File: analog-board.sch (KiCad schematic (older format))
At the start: 496 parts, among them J1 AC IN, J2 OUT, J3 CONN_20X2, P2 CONN_01X02, Q1 2N3906, Q10 2N3906, Q11 2N3906, Q12 2N3906, Q13 2N3906, Q14 2N3906, Q15 2N3906, Q16 2N3906, Q17 NPN, Q18 NPN, Q19 J111, Q2 2N3906, Q20 2N3906, Q3 2N3906, Q4 2N3906, Q5 2N3906, Q6 BCM857BS, Q7 2N3906, Q8 2N3906, Q9 2N3906, U1 LM13700, U10 ADR01, U11 DG212B, U12 DG212B, U13 DG408, U14 DG408, U15 TL072-, U16 DG408, U17 DG408, U18 LM13700, U19 LM13700, U2 LM13700, U20 74HC75, U21 TL072-, U22 TL074-, U23 TL074-, U24 TL074-, U25 TL074-, U26 TL072-, U27 TL074-, U28 TL074-, U29 LM13700, U3 LM13700, U30 LM13700, U31 TL074-, U32 LM13700, U33 TL074-, U34 TL074-, U35 TL074-, U36 74LV573, U38 0 - 10V, U39 TL074-, U4 DG212B, U40 DG419, U41 0 - 10V, U42 10 - 0V, U43 LM7812, U44 LM7912, U45 DG408, U46 7805, U5 TL074-, U6 AD5556, U7 TL072-, U8 TL074-, U9 AD8672

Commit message: LFO TUNE now connected to S&H clock through R215
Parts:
- added R215: 10K, symbol R_US
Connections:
- net LFO TUNE: now also R215.1; no longer C102.1, LFO1.9, R210.2
- net at D4.2 (K), TP25.1, U39.8: now also R215.2
- new net: C102.1, LFO1.9, R210.2
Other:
- note added: "*NOTE: C47 and C48 values: need\nto experiment more with C47 and \nC48 values. Changee to dual\nfootprint 0805 and TH."
- note added: "Can probably\nget rid of mixer\nVCA trimmers"
- note added: "Can probably\nget rid of volume\nVCA trimmer"
- note added: "Move C100 to after\nvolume VCA?"
- note added: "NP0 or FILM\n"
- note added: "S&H CLOCK"
- note removed: "*NOTE: C47 and C48 values: need\nto experiment more with C47 and \nC48 values. Change to dual\nfootprint 0805 and TH."
- note removed: "NP0 or FILM\nNeed to change to larger footprint here!"
- note removed: "Need to change to\nlarger footprint here!"
- moved on the sheet: TP25
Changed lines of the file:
@@
 $EndComp
 Text Notes 39000 7350 0    60   ~ 0
-NP0 or FILM\nNeed to change to larger footprint here!
+NP0 or FILM\n
 $Comp
 L GND #PWR0114
@@
 L CONN_1 TP25
 U 1 1 5453F2E4
-P 38450 8050
-F 0 "TP25" H 38530 8050 40  0000 L CNN
-F 1 "CONN_1" H 38450 8150 30  0001 C CNN
-F 2 "~" H 38450 8050 60  0000 C CNN
-F 3 "~" H 38450 8050 60  0000 C CNN
-	1    38450 8050
-	1    0    0    -1
+P 38650 7700
+F 0 "TP25" H 38730 7700 40  0000 L CNN
+F 1 "CONN_1" H 38650 7800 30  0001 C CNN
+F 2 "~" H 38650 7700 60  0000 C CNN
+F 3 "~" H 38650 7700 60  0000 C CNN
+	1    38650 7700
+	0    -1   -1   0
 $EndComp
-Text GLabel 36400 4700 2    60   Output ~ 0
-LFO TUNE
 Text Notes 40500 3900 0    60   ~ 0
 S&H
@@
 Text Notes 42450 7050 1    60   ~ 0
 Note: for ease of PCB layout order\nof mux addressing is not sequential
-Text Notes 18400 9150 0    60   ~ 0
-Need to change to\nlarger footprint here!
-Text Notes 18300 11000 0    60   ~ 0
-Need to change to\nlarger footprint here!
 Text Notes 14600 13800 0    60   ~ 0
 Changed to 47K to\nprevent clipping
@@
 *NOTE: jumper 1K output resistor\non EG2 module; it forms a divider \nwith input resistors to EG2 \nmodulation depth VCAs
 Text Notes 16450 11100 0    60   ~ 0
-*NOTE: C47 and C48 values: need\nto experiment more with C47 and \nC48 values. Change to dual\nfootprint 0805 and TH.
+*NOTE: C47 and C48 values: need\nto experiment more with C47 and \nC48 values. Changee to dual\nfootprint 0805 and TH.
 Text Notes 31500 31750 0    60   ~ 0
 External gate input doesn't work here.\nProbably because OR gate on digital board\ncan sink and source current, so holds output \nlow when external gate is applied?
@@
 Connection ~ 37000 8150
 Wire Wire Line
-	31650 4700 36400 4700
-Wire Wire Line
 	31650 4700 31650 8150
 Wire Wire Line
 	31650 8150 35900 8150
 Connection ~ 40250 5950
-Connection ~ 36150 4700
 Wire Wire Line
 	42200 4600 42200 5200
@@
 Text Notes 12300 20800 0    60   ~ 0
 PULSE output\ndivider network\nto get 10 Vpp
+$Comp
+L R_US R215
+U 1 1 559CB5A4
+P 39000 8050
+F 0 "R215" V 39080 8050 50  0000 C CNN
+F 1 "10K" V 38920 8050 50  0000 C CNN
+F 2 "" H 39000 8050 60  0000 C CNN
+F 3 "" H 39000 8050 60  0000 C CNN
+	1    39000 8050
+	0    1    1    0
+$EndComp
+Text GLabel 39300 8050 2    60   Output ~ 0
+LFO TUNE
+Wire Wire Line
+	38300 8050 38800 8050
+Wire Wire Line
+	38650 7850 38650 8050
+Connection ~ 38650 8050
+Text Notes 38750 7750 0    60   ~ 0
+S&H CLOCK
+Wire Wire Line
+	39200 8050 39300 8050
+Wire Wire Line
+	36150 4700 31650 4700
+Text Notes 17650 15850 0    60   ~ 0
+Can probably\nget rid of mixer\nVCA trimmers
+Text Notes 19500 18150 0    60   ~ 0
+Can probably\nget rid of mixer\nVCA trimmers
+Text Notes 17600 20750 0    60   ~ 0
+Can probably\nget rid of mixer\nVCA trimmers
+Text Notes 37650 17800 0    60   ~ 0
+Can probably\nget rid of volume\nVCA trimmer
+Text Notes 38650 16500 0    60   ~ 0
+Can probably\nget rid of volume\nVCA trimmer
+Text Notes 35450 16200 0    60   ~ 0
+Move C100 to after\nvolume VCA?
 $EndSCHEMATC

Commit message: moved final DC blocking cap to output of volume VCA, deleted ring output resistor to J2
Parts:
- removed R205: 1K, symbol R_US
- added C134: 22µ, ~, symbol CP_US
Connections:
- net at C111.1, R202.2, R204.1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: no longer TP26.1
- net at R200.2, U32.5: now also C134.1 (+); no longer R202.1
- new net: C134.2 (-), R202.1, TP26.1
- no-connect marks 17 -> 18
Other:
- note added: "Jumper C100 and try\nC134 as DC blocker"
- note added: "Plugging TS jack in shorts ring to GND\nSo dual output to ring has been removed"
- note added: "Where did the idea for \nthis final buffer come \nfrom? P5 uses non-\ninverting buffer. This\nlooks more like JP8\noutput amplifier."
- note removed: "J2 pins mixed up, results in \noutput being shorted to ground!"
- note removed: "Move C100 to after\nvolume VCA?"
- moved on the sheet: C111, J2, R202, R204, R39, TP26, U35D
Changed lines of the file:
@@
 L R_US R39
 U 1 1 5453E97B
-P 40700 16750
-F 0 "R39" V 40900 16750 50  0000 C CNN
-F 1 "1K" V 40800 16750 50  0000 C CNN
-F 2 "" H 40700 16750 60  0000 C CNN
-F 3 "" H 40700 16750 60  0000 C CNN
-	1    40700 16750
+P 41150 16750
+F 0 "R39" V 41350 16750 50  0000 C CNN
+F 1 "1K" V 41250 16750 50  0000 C CNN
+F 2 "" H 41150 16750 60  0000 C CNN
+F 3 "" H 41150 16750 60  0000 C CNN
+	1    41150 16750
 	0    -1   -1   0
 $EndComp
@@
 L GND #PWR073
 U 1 1 5453EA14
-P 39250 17050
-F 0 "#PWR073" H 39250 17050 30  0001 C CNN
-F 1 "GND" H 39250 16980 30  0001 C CNN
-F 2 "~" H 39250 17050 60  0000 C CNN
-F 3 "~" H 39250 17050 60  0000 C CNN
-	1    39250 17050
+P 39700 17050
+F 0 "#PWR073" H 39700 17050 30  0001 C CNN
+F 1 "GND" H 39700 16980 30  0001 C CNN
+F 2 "~" H 39700 17050 60  0000 C CNN
+F 3 "~" H 39700 17050 60  0000 C CNN
+	1    39700 17050
 	1    0    0    -1
 $EndComp
@@
 L R_US R204
 U 1 1 5453EA1A
-P 39900 15800
-F 0 "R204" V 39980 15800 50  0000 C CNN
-F 1 "100K" V 39820 15800 50  0000 C CNN
-F 2 "" H 39900 15800 60  0000 C CNN
-F 3 "" H 39900 15800 60  0000 C CNN
-	1    39900 15800
+P 40350 15750
+F 0 "R204" V 40430 15750 50  0000 C CNN
+F 1 "100K" V 40270 15750 50  0000 C CNN
+F 2 "" H 40350 15750 60  0000 C CNN
+F 3 "" H 40350 15750 60  0000 C CNN
+	1    40350 15750
 	0    -1   -1   0
 $EndComp
@@
 L C_US C111
 U 1 1 5453EA20
-P 39900 15450
-F 0 "C111" H 39950 15550 50  0000 L CNN
-F 1 "100pF" H 39950 15350 50  0000 L CNN
-F 2 "~" H 39900 15450 60  0000 C CNN
-F 3 "~" H 39900 15450 60  0000 C CNN
-	1    39900 15450
+P 40350 15450
+F 0 "C111" H 40400 15550 50  0000 L CNN
+F 1 "100pF" H 40400 15350 50  0000 L CNN
+F 2 "~" H 40350 15450 60  0000 C CNN
+F 3 "~" H 40350 15450 60  0000 C CNN
+	1    40350 15450
 	0    -1   -1   0
 $EndComp
@@
 L JACK_MONO_SW J2
 U 1 1 5453EA99
-P 41250 16900
-F 0 "J2" H 40700 16800 60  0000 C CNN
-F 1 "OUT" H 41000 17100 60  0000 C CNN
-F 2 "~" H 41150 16900 60  0000 C CNN
-F 3 "~" H 41150 16900 60  0000 C CNN
-	1    41250 16900
+P 41700 16900
+F 0 "J2" H 41150 16800 60  0000 C CNN
+F 1 "OUT" H 41450 17100 60  0000 C CNN
+F 2 "~" H 41600 16900 60  0000 C CNN
+F 3 "~" H 41600 16900 60  0000 C CNN
+	1    41700 16900
 	-1   0    0    1
 $EndComp
@@
 L GND #PWR082
 U 1 1 5453EAA0
-P 40900 17250
-F 0 "#PWR082" H 40900 17250 30  0001 C CNN
-F 1 "GND" H 40900 17180 30  0001 C CNN
-F 2 "~" H 40900 17250 60  0000 C CNN
-F 3 "~" H 40900 17250 60  0000 C CNN
-	1    40900 17250
+P 41350 17250
+F 0 "#PWR082" H 41350 17250 30  0001 C CNN
+F 1 "GND" H 41350 17180 30  0001 C CNN
+F 2 "~" H 41350 17250 60  0000 C CNN
+F 3 "~" H 41350 17250 60  0000 C CNN
+	1    41350 17250
 	1    0    0    -1
 $EndComp
@@
 L R_US R202
 U 1 1 546C49C0
-P 38900 16650
-F 0 "R202" V 38980 16650 50  0000 C CNN
-F 1 "100K" V 38820 16650 50  0000 C CNN
-F 2 "" H 38900 16650 60  0000 C CNN
-F 3 "" H 38900 16650 60  0000 C CNN
-	1    38900 16650
+P 39350 16650
+F 0 "R202" V 39430 16650 50  0000 C CNN
+F 1 "100K" V 39270 16650 50  0000 C CNN
+F 2 "" H 39350 16650 60  0000 C CNN
+F 3 "" H 39350 16650 60  0000 C CNN
+	1    39350 16650
 	0    -1   -1   0
 $EndComp
@@
 L CONN_1 TP26
 U 1 1 546C5BBD
-P 39250 15300
-F 0 "TP26" H 39330 15300 40  0000 L CNN
-F 1 "CONN_1" H 39250 15400 30  0001 C CNN
-F 2 "~" H 39250 15300 60  0000 C CNN
-F 3 "~" H 39250 15300 60  0000 C CNN
-	1    39250 15300
+P 39100 15350
+F 0 "TP26" H 39180 15350 40  0000 L CNN
+F 1 "CONN_1" H 39100 15450 30  0001 C CNN
+F 2 "~" H 39100 15350 60  0000 C CNN
+F 3 "~" H 39100 15350 60  0000 C CNN
+	1    39100 15350
 	0    -1   -1   0
 $EndComp
@@
 L TL074- U35
 U 4 1 548B1C06
-P 39850 16750
-F 0 "U35" H 39900 16950 60  0000 C CNN
-F 1 "TL074-" H 40000 16550 50  0000 C CNN
-F 2 "~" H 39850 16750 60  0000 C CNN
-F 3 "~" H 39850 16750 60  0000 C CNN
-	4    39850 16750
+P 40300 16750
+F 0 "U35" H 40350 16950 60  0000 C CNN
+F 1 "TL074-" H 40450 16550 50  0000 C CNN
+F 2 "~" H 40300 16750 60  0000 C CNN
+F 3 "~" H 40300 16750 60  0000 C CNN
+	4    40300 16750
 	1    0    0    -1
 $EndComp
@@
 NoConn ~ 37150 24250
 $Comp
-L R_US R205
-U 1 1 549A3192
-P 40700 16900
-F 0 "R205" V 40550 16900 50  0000 C CNN
-F 1 "1K" V 40620 16900 50  0000 C CNN
-F 2 "" H 40700 16900 60  0000 C CNN
-F 3 "" H 40700 16900 60  0000 C CNN
-	1    40700 16900
-	0    -1   -1   0
-$EndComp
-$Comp
 L CONN_01X02 P2
 U 1 1 54961D96
@@
 Text Notes 6000 24250 0    60   ~ 0
 bias PWM MOD \nCVs down -5V
-Text Notes 40700 16450 0    60   ~ 0
-J2 pins mixed up, results in \noutput being shorted to ground!
+Text Notes 41150 16450 0    60   ~ 0
+Plugging TS jack in shorts ring to GND\nSo dual output to ring has been removed
 Text Notes 35600 30650 0    60   ~ 0
 *NOTE: jumper 1K output resistor\non EG2 module; it forms a divider \nwith input resistors to EG2 \nmodulation depth VCAs
@@
 	35200 16500 35450 16500
 Wire Wire Line
-	39100 16650 39350 16650
+	39550 16650 39800 16650
 Wire Wire Line
-	39350 16850 39250 16850
+	39800 16850 39700 16850
 Wire Wire Line
-	39250 16850 39250 17050
+	39700 16850 39700 17050
 Wire Wire Line
-	39700 15800 39250 15800
+	40150 15750 39700 15750
 Wire Wire Line
-	39250 15450 39250 16650
-Connection ~ 39250 16650
+	39700 15450 39700 16650
+Connection ~ 39700 16650
 Wire Wire Line
-	40100 15800 40500 15800
+	40550 15750 40950 15750
 Wire Wire Line
-	40500 15450 40500 16900
+	40150 15450 39700 15450
+Connection ~ 39700 15750
 Wire Wire Line
-	39700 15450 39250 15450
-Connection ~ 39250 15800
-Wire Wire Line
-	40100 15450 40500 15450
-Connection ~ 40500 15800
+	40550 15450 40950 15450
+Connection ~ 40950 15750
 Wire Wire Line
 	35850 16500 35950 16500
@@
 	35000 3900 35000 4050
 Wire Wire Line
-	41000 17050 40900 17050
+	41450 17050 41350 17050
 Wire Wire Line
-	40900 17050 40900 17250
+	41350 17050 41350 17250
 Wire Wire Line
 	12150 19900 12150 20650
@@
 	33750 21350 33750 18850
 Wire Wire Line
-	40500 16750 40350 16750
-Connection ~ 40500 16750
+	40950 16750 40800 16750
+Connection ~ 40950 16750
 Wire Notes Line
 	29900 27600 37400 27600
@@
 	38200 15500 38200 15800
 Wire Wire Line
-	38350 16650 38700 16650
+	38350 16650 38650 16650
 Wire Wire Line
 	38500 16650 38500 16850
@@
 	37150 17700 37250 17700
 Wire Wire Line
-	41000 16750 40900 16750
+	41450 16750 41350 16750
 Wire Wire Line
 	27200 28600 27000 28600
@@
 	5250 23600 5250 23550
 Wire Wire Line
-	41000 16900 40900 16900
+	41450 16900 41350 16900
 Wire Wire Line
 	37550 23400 39250 23400
@@
 Text Notes 37650 17800 0    60   ~ 0
 Can probably\nget rid of volume\nVCA trimmer
-Text Notes 38650 16500 0    60   ~ 0
-Can probably\nget rid of volume\nVCA trimmer
 Text Notes 35450 16200 0    60   ~ 0
-Move C100 to after\nvolume VCA?
+Jumper C100 and try\nC134 as DC blocker
+$Comp
+L CP_US C134
+U 1 1 55A0FDA4
+P 38850 16650
+F 0 "C134" H 38900 16750 50  0000 L CNN
+F 1 "22µ" H 38900 16550 50  0000 L CNN
+F 2 "~" H 38850 16650 60  0000 C CNN
+F 3 "~" H 38850 16650 60  0000 C CNN
+	1    38850 16650
+	0    -1   -1   0
+$EndComp
+Wire Wire Line
+	40950 15450 40950 16750
+NoConn ~ 41350 16900
+Text Notes 39800 16450 0    60   ~ 0
+Where did the idea for \nthis final buffer come \nfrom? P5 uses non-\ninverting buffer. This\nlooks more like JP8\noutput amplifier.
+Wire Wire Line
+	39050 16650 39150 16650
+Wire Wire Line
+	39100 15500 39100 16650
+Connection ~ 39100 16650
 $EndSCHEMATC

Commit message: added note about changing R11 and R117 to 470K for VCO1 and FIL cutoff modulation by EG2
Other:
- note added: "Changed to 470K\nto minimize offset"
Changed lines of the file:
@@
 LIBS:MySynthParts
 LIBS:analog-board-cache
-EELAYER 25 0
+EELAYER 24 0
 EELAYER END
 $Descr E 44000 34000
@@
 	39100 15500 39100 16650
 Connection ~ 39100 16650
+Text Notes 2500 7650 0    60   ~ 0
+Changed to 470K\nto minimize offset
+Text Notes 24600 8700 0    60   ~ 0
+Changed to 470K\nto minimize offset
 $EndSCHEMATC

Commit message: added TUNE COMPARATOR in schematic, need to route in PCB
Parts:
- added C?: 10p, ~, symbol C_US
- added D?: 1N4148, ~, symbol DIODE
- added R?: 270K, ~, symbol R_US
- added R?: 22K, ~, symbol R_US
- added R?: 10K, ~, symbol R_US
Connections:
- net +12V: now also R?.2
- net GND: now also R?.1, R?.2; no longer U26.5 (+)
- net TUNE: now also D?.2 (K), R?.2; no longer C100.1 (+), TP24.1, VCFA1.10 (OUT)
- net at U26.6 (-): now also R?.1, R?.1; no longer U26.7
- new net: C100.1 (+), C?.1, TP24.1, U26.5 (+), VCFA1.10 (OUT)
- new net: C?.2, D?.1 (A), U26.7
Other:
- note added: "TUNE COMPARATOR"
- moved on the sheet: U26B
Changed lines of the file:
@@
 Text GLabel 15250 31400 0    40   Input ~ 0
 DB2
-Text GLabel 35950 16850 2    60   Output ~ 0
+Text GLabel 39450 19500 2    60   Output ~ 0
 TUNE
 Text Notes 31400 1500 0    60   ~ 0
@@
 $EndComp
 $Comp
-L GND #PWR0309
-U 1 1 548A1FC7
-P 22150 19200
-F 0 "#PWR0309" H 22150 19200 30  0001 C CNN
-F 1 "GND" H 22150 19130 30  0001 C CNN
-F 2 "~" H 22150 19200 60  0000 C CNN
-F 3 "~" H 22150 19200 60  0000 C CNN
-	1    22150 19200
-	1    0    0    -1
-$EndComp
-Text Notes 22500 18450 0    60   ~ 0
-SPARE
-$Comp
 L TL072- U26
 U 2 1 548A1FE3
-P 22650 18850
-F 0 "U26" H 22600 19050 60  0000 L CNN
-F 1 "TL072-" H 22600 18600 60  0000 L CNN
-F 2 "~" H 22650 18850 60  0000 C CNN
-F 3 "~" H 22650 18850 60  0000 C CNN
-	2    22650 18850
+P 37900 19500
+F 0 "U26" H 37850 19700 60  0000 L CNN
+F 1 "TL072-" H 37850 19250 60  0000 L CNN
+F 2 "~" H 37900 19500 60  0000 C CNN
+F 3 "~" H 37900 19500 60  0000 C CNN
+	2    37900 19500
 	1    0    0    -1
 $EndComp
@@
 	8350 24150 8350 24500
 Wire Wire Line
-	22150 18950 22150 19200
-Wire Wire Line
-	22150 18750 22150 18500
-Wire Wire Line
-	22150 18500 23150 18500
-Wire Wire Line
-	23150 18500 23150 18850
-Wire Wire Line
 	27750 5400 28050 5400
 Connection ~ 28050 5750
@@
 Text Notes 24600 8700 0    60   ~ 0
 Changed to 470K\nto minimize offset
+Wire Wire Line
+	35950 16850 35950 19600
+Wire Wire Line
+	35950 19600 37400 19600
+$Comp
+L R_US R?
+U 1 1 55BDADA6
+P 37350 18850
+F 0 "R?" V 37430 18850 50  0000 C CNN
+F 1 "270K" V 37270 18850 50  0000 C CNN
+F 2 "~" H 37350 18850 60  0000 C CNN
+F 3 "~" H 37350 18850 60  0000 C CNN
+	1    37350 18850
+	0    -1   -1   0
+$EndComp
+$Comp
+L C_US C?
+U 1 1 55BDB02B
+P 37900 20150
+F 0 "C?" H 37950 20250 50  0000 L CNN
+F 1 "10p" H 37950 20050 50  0000 L CNN
+F 2 "~" H 37900 20150 60  0000 C CNN
+F 3 "~" H 37900 20150 60  0000 C CNN
+	1    37900 20150
+	0    -1   -1   0
+$EndComp
+Wire Wire Line
+	37200 19600 37200 20150
+Wire Wire Line
+	37200 20150 37700 20150
+Connection ~ 37200 19600
+Wire Wire Line
+	38100 20150 38550 20150
+Wire Wire Line
+	38550 20150 38550 19500
+Wire Wire Line
+	38550 19500 38400 19500
+$Comp
+L DIODE D?
+U 1 1 55BDDA0C
+P 38750 19500
+F 0 "D?" H 38750 19600 40  0000 C CNN
+F 1 "1N4148" H 38750 19400 40  0000 C CNN
+F 2 "~" H 38750 19500 60  0000 C CNN
+F 3 "~" H 38750 19500 60  0000 C CNN
+	1    38750 19500
+	1    0    0    -1
+$EndComp
+$Comp
+L R_US R?
+U 1 1 55BE103B
+P 39100 19800
+F 0 "R?" V 39180 19800 50  0000 C CNN
+F 1 "22K" V 39020 19800 50  0000 C CNN
+F 2 "~" H 39100 19800 60  0000 C CNN
+F 3 "~" H 39100 19800 60  0000 C CNN
+	1    39100 19800
+	-1   0    0    1
+$EndComp
+$Comp
+L GND #PWR?
+U 1 1 55BE12C5
+P 39100 20200
+F 0 "#PWR?" H 39100 20200 30  0001 C CNN
+F 1 "GND" H 39100 20130 30  0001 C CNN
+F 2 "~" H 39100 20200 60  0000 C CNN
+F 3 "~" H 39100 20200 60  0000 C CNN
+	1    39100 20200
+	1    0    0    -1
+$EndComp
+Wire Wire Line
+	39100 20000 39100 20200
+Wire Wire Line
+	38950 19500 39450 19500
+Wire Wire Line
+	39100 19500 39100 19600
+Connection ~ 39100 19500
+$Comp
+L R_US R?
+U 1 1 55BE3A1D
+P 36750 18850
+F 0 "R?" V 36830 18850 50  0000 C CNN
+F 1 "10K" V 36670 18850 50  0000 C CNN
+F 2 "~" H 36750 18850 60  0000 C CNN
+F 3 "~" H 36750 18850 60  0000 C CNN
+	1    36750 18850
+	0    1    1    0
+$EndComp
+Wire Wire Line
+	37400 19400 37050 19400
+Wire Wire Line
+	37050 19400 37050 18850
+Wire Wire Line
+	36950 18850 37150 18850
+Connection ~ 37050 18850
+$Comp
+L GND #PWR?
+U 1 1 55BE8FD3
+P 36550 19050
+F 0 "#PWR?" H 36550 19050 30  0001 C CNN
+F 1 "GND" H 36550 18980 30  0001 C CNN
+F 2 "~" H 36550 19050 60  0000 C CNN
+F 3 "~" H 36550 19050 60  0000 C CNN
+	1    36550 19050
+	1    0    0    -1
+$EndComp
+Wire Wire Line
+	36550 18850 36550 19050
+$Comp
+L +12V #PWR?
+U 1 1 55BE9ACA
+P 37700 18750
+F 0 "#PWR?" H 37700 18850 30  0001 C CNN
+F 1 "+12V" H 37675 19025 60  0000 C CNN
+F 2 "~" H 37700 18750 60  0000 C CNN
+F 3 "~" H 37700 18750 60  0000 C CNN
+	1    37700 18750
+	1    0    0    -1
+$EndComp
+Wire Wire Line
+	37550 18850 37700 18850
+Wire Wire Line
+	37700 18850 37700 18750
+Text Notes 37950 19100 0    60   ~ 0
+TUNE COMPARATOR
 $EndSCHEMATC

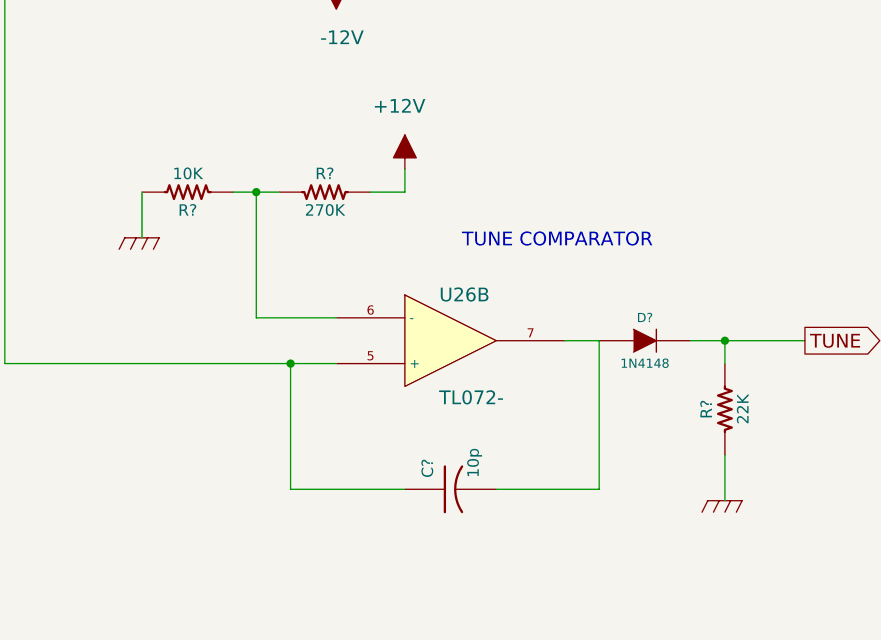
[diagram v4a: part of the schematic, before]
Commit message: routed tune comparator
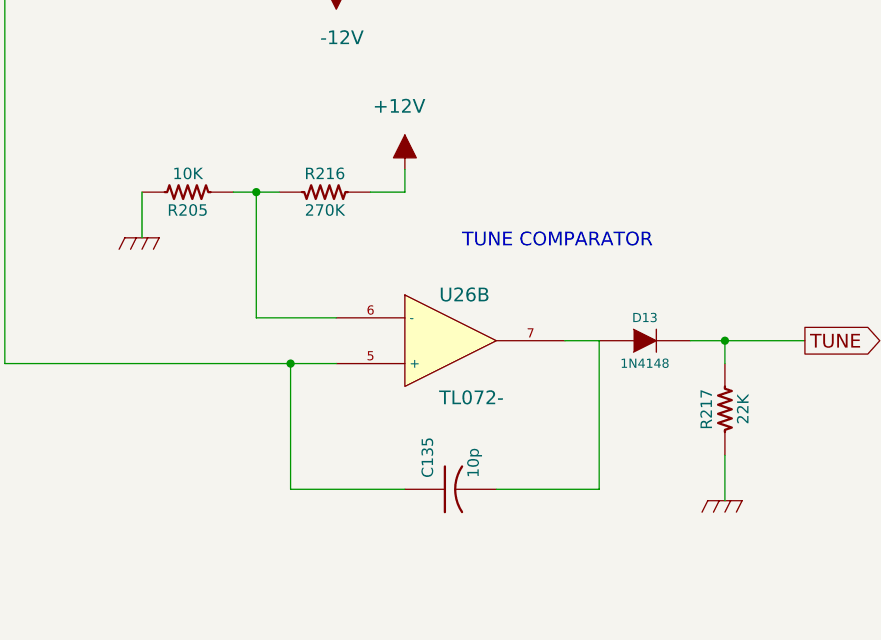
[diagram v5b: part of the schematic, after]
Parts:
- gave numbers to parts that had none: 5

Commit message: basically done. need to do last quick check of a few footprints, but otherwise board is ready to order. Will place order upon returning from Lighthouse
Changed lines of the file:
@@
 LIBS:MySynthParts
 LIBS:analog-board-cache
-EELAYER 24 0
+EELAYER 25 0
 EELAYER END
 $Descr E 44000 34000
@@
 Text Notes 37950 19100 0    60   ~ 0
 TUNE COMPARATOR
+Text Notes 35000 23300 0    60   ~ 0
+SPARE
 $EndSCHEMATC

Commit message: few touch ups and silkscreen corrections. Ready to order from Seeed Studio
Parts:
- C135: value 10p -> 47p
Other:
- note added: "C135 changed from 10pF to 47pF\non breadboard to improve clock\nedge"
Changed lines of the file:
@@
 P 37900 20150
 F 0 "C135" H 37950 20250 50  0000 L CNN
-F 1 "10p" H 37950 20050 50  0000 L CNN
+F 1 "47p" H 37950 20050 50  0000 L CNN
 F 2 "~" H 37900 20150 60  0000 C CNN
 F 3 "~" H 37900 20150 60  0000 C CNN
@@
 Text Notes 35000 23300 0    60   ~ 0
 SPARE
+Text Notes 37150 20550 0    60   ~ 0
+C135 changed from 10pF to 47pF\non breadboard to improve clock\nedge
 $EndSCHEMATC
